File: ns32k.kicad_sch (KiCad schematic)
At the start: 49 parts, among them SW2 SW_DIP_x04, U1 NS32201, U10 74AHC373, U11 74AHC373, U12 74AHC138, U13 AS6C6416-55, U15 MX29LV040C, U16 MX29LV040C, U19 74AHC32, U20 74AHC1GU04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

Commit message: layout ICU buffering
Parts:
- added C58: 0.1µF, Capacitor_SMD:C_0402_1005Metric, symbol Device:C_Small
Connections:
- net +3V3: now also C58.1
- net D0: no longer U22.18 (B0), U5.19 (D0)
- net D1: no longer U22.17 (B1), U5.18 (D1)
- net D2: no longer U22.16 (B2), U5.17 (D2)
- net D3: no longer U22.15 (B3), U5.16 (D3)
- net D4: no longer U22.14 (B4), U5.15 (D4)
- net D5: no longer U22.13 (B5), U5.14 (D5)
- net D6: no longer U22.12 (B6), U5.13 (D6)
- net D7: no longer U22.11 (B7), U5.12 (D7)
- net GND: now also C58.2
- new net: U22.11 (B7), U5.12 (D7)
- new net: U22.12 (B6), U5.13 (D6)
- new net: U22.13 (B5), U5.14 (D5)
- new net: U22.14 (B4), U5.15 (D4)
- new net: U22.15 (B3), U5.16 (D3)
- new net: U22.16 (B2), U5.17 (D2)
- new net: U22.17 (B1), U5.18 (D1)
- new net: U22.18 (B0), U5.19 (D0)
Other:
- moved on the sheet: U19B, U20

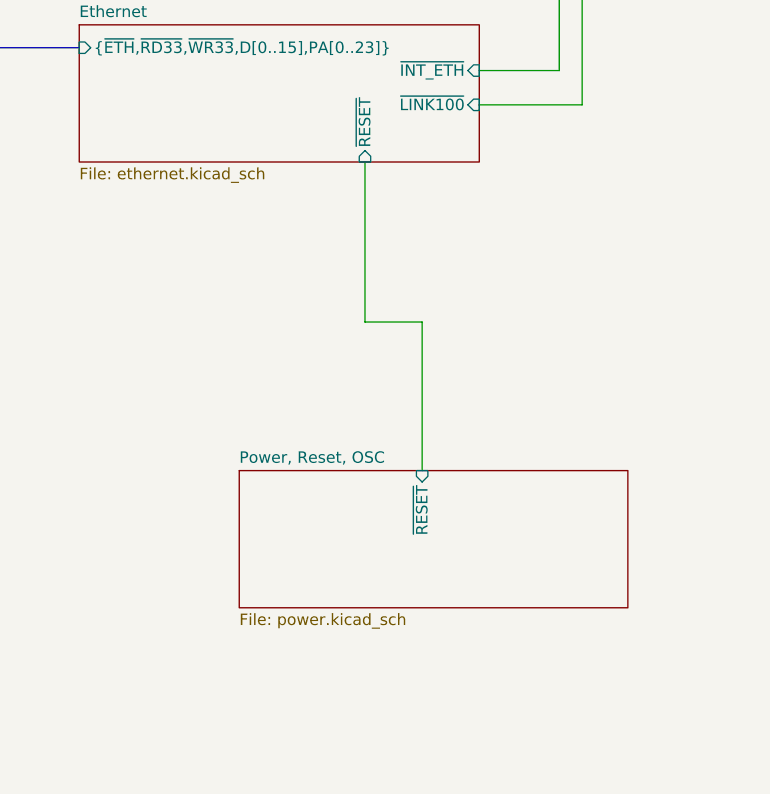
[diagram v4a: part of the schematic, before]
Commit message: add 33uF 1206 16V reservoir cap to 5V
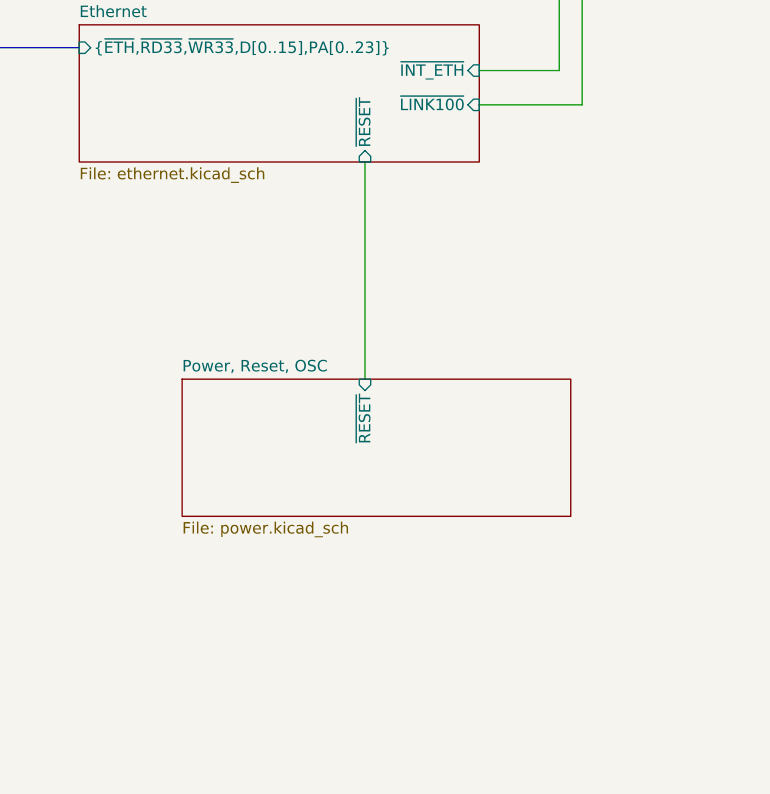
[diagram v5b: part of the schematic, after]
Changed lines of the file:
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@@
 	(wire
 		(pts
-			(xy 359.41 212.09) (xy 359.41 194.31)
+			(xy 359.41 194.31) (xy 359.41 218.44)
 		)
 		(stroke
@@
 	(wire
 		(pts
-			(xy 365.76 212.09) (xy 359.41 212.09)
-		)
-		(stroke
-			(width 0)
-			(type default)
-		)
-	)
-	(wire
-		(pts
 			(xy 187.96 91.44) (xy 187.96 93.98)
 		)
@@
 		)
 	)
-	(wire
-		(pts
-			(xy 365.76 228.6) (xy 365.76 212.09)
-		)
-		(stroke
-			(width 0)
-			(type default)
-		)
-	)
 	(bus
 		(pts
@@
 	(label "PA5"
 		(at 300.99 77.47 180)
+		(fields_autoplaced yes)
 		(effects
 			(font
@@
 	(label "~{ICU}"
 		(at 298.45 57.15 180)
+		(fields_autoplaced yes)
 		(effects
 			(font
@@
 	(label "~{ICU}"
 		(at 287.02 74.93 0)
+		(fields_autoplaced yes)
 		(effects
 			(font
@@
 	(label "~{ICU}"
 		(at 232.41 158.75 0)
+		(fields_autoplaced yes)
 		(effects
 			(font
@@
 	(label "~{DBE}"
 		(at 238.76 73.66 90)
+		(fields_autoplaced yes)
 		(effects
 			(font
@@
 	)
 	(sheet
-		(at 345.44 228.6)
+		(at 339.09 218.44)
 		(size 43.18 15.24)
 		(fields_autoplaced yes)
@@
 		)
 		(property "Sheetname" "Power, Reset, OSC"
-			(at 345.44 227.8884 0)
+			(at 339.09 217.7284 0)
 			(effects
 				(font
@@
 		)
 		(property "Sheetfile" "power.kicad_sch"
-			(at 345.44 244.4246 0)
+			(at 339.09 234.2646 0)
 			(effects
 				(font
@@
 		)
 		(pin "~{RESET}" input
-			(at 365.76 228.6 90)
+			(at 359.41 218.44 90)
 			(effects
 				(font

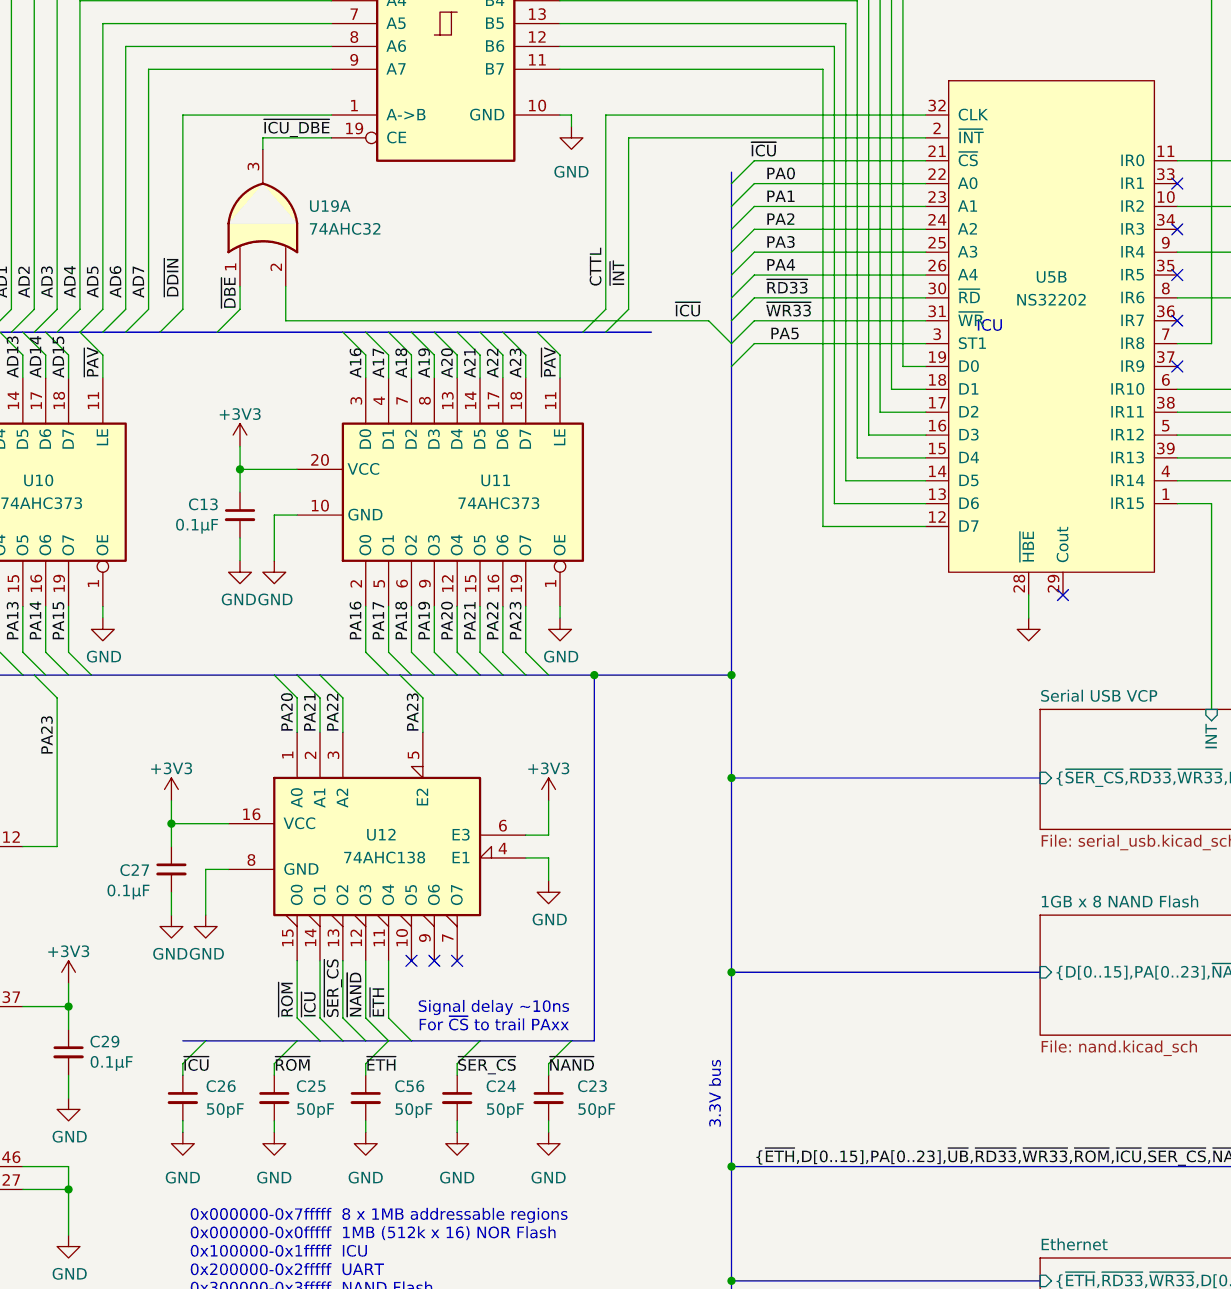
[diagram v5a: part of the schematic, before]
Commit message: fix ICU addressing error
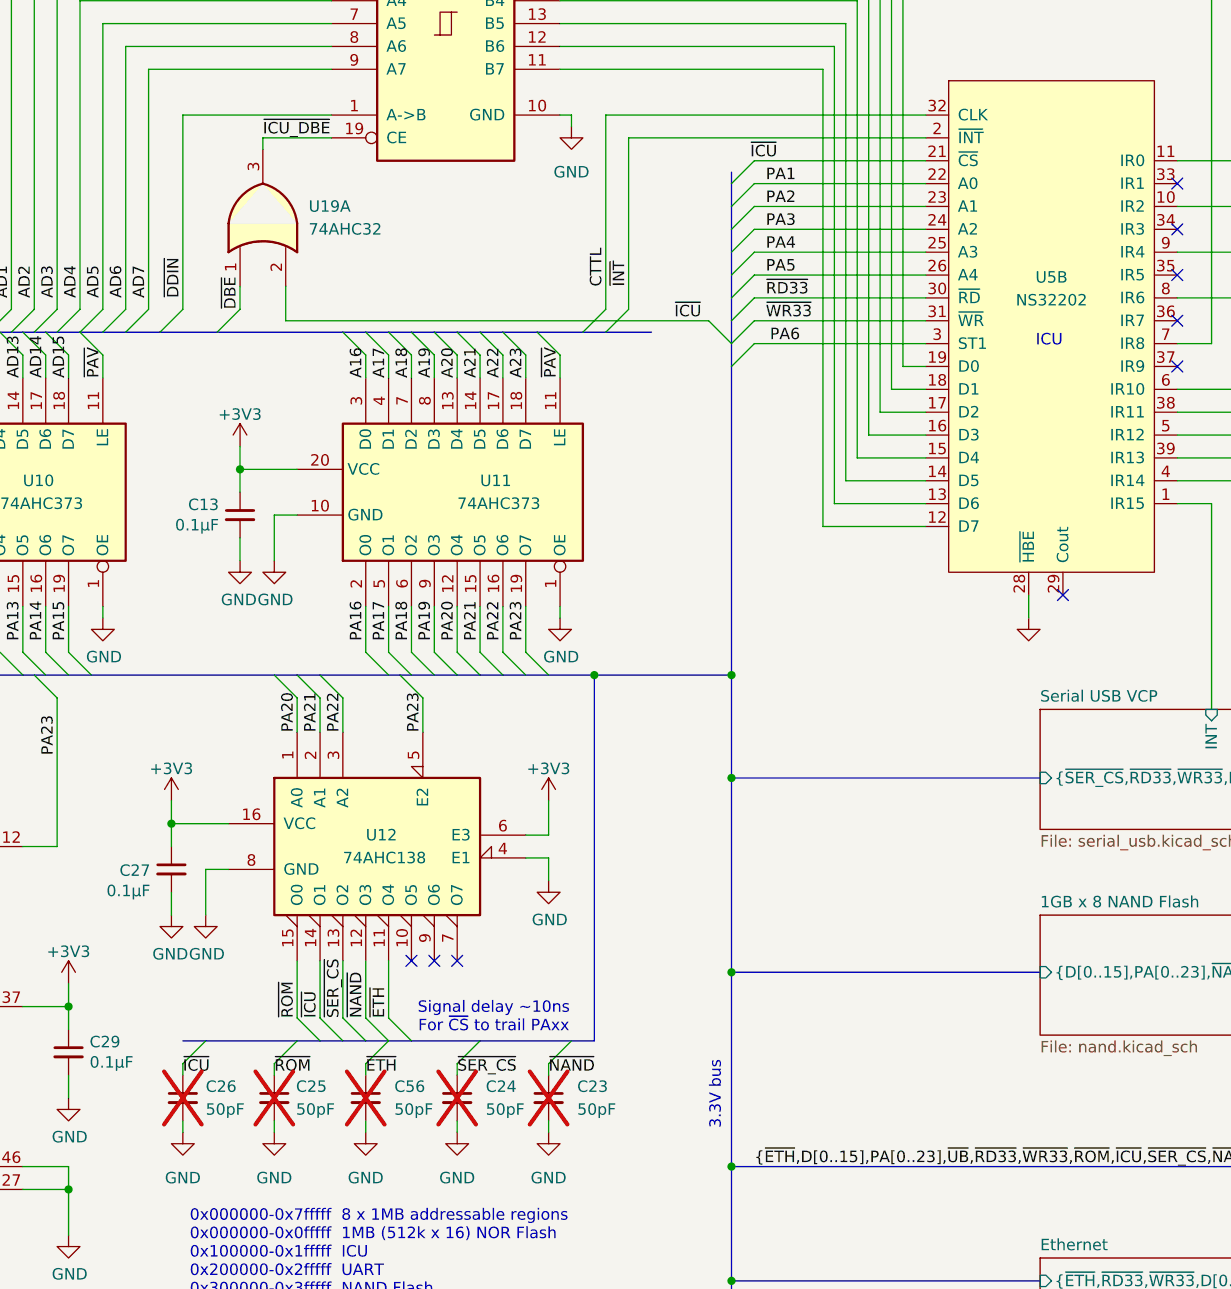
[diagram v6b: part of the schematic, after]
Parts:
- C23, C24, C25, C26, C56: now not fitted
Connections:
- net PA0: no longer U5.22 (A0)
- net PA1: now also U5.22 (A0); no longer U5.23 (A1)
- net PA2: now also U5.23 (A1); no longer U5.24 (A2)
- net PA3: now also U5.24 (A2); no longer U5.25 (A3)
- net PA4: now also U5.25 (A3); no longer U5.26 (A4)
- net PA5: now also U5.26 (A4); no longer U5.3 (ST1)
- net PA6: now also U5.3 (ST1)
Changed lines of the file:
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@@
 	(text "ICU"
 		(exclude_from_sim no)
-		(at 322.072 75.692 0)
+		(at 328.676 77.216 0)
 		(effects
 			(font
@@
 		)
 	)
-	(label "PA4"
+	(label "PA5"
 		(at 297.18 69.85 0)
 		(fields_autoplaced yes)
@@
 		)
 	)
-	(label "PA5"
+	(label "PA6"
 		(at 300.99 77.47 180)
 		(fields_autoplaced yes)
@@
 		)
 	)
-	(label "PA2"
+	(label "PA3"
 		(at 297.18 64.77 0)
 		(fields_autoplaced yes)
@@
 		)
 	)
-	(label "PA3"
+	(label "PA4"
 		(at 297.18 67.31 0)
 		(fields_autoplaced yes)
@@
 		)
 	)
-	(label "PA0"
+	(label "PA1"
 		(at 297.18 59.69 0)
 		(fields_autoplaced yes)
@@
 		)
 	)
-	(label "PA1"
+	(label "PA2"
 		(at 297.18 62.23 0)
 		(fields_autoplaced yes)
@@
 		(in_bom yes)
 		(on_board yes)
-		(dnp no)
+		(dnp yes)
 		(property "Reference" "C56"
 			(at 255.905 160.0262 0)
@@
 		(in_bom yes)
 		(on_board yes)
-		(dnp no)
+		(dnp yes)
 		(property "Reference" "C24"
 			(at 266.065 160.0262 0)
@@
 		(in_bom yes)
 		(on_board yes)
-		(dnp no)
+		(dnp yes)
 		(property "Reference" "C26"
 			(at 234.95 160.02 0)
@@
 		(in_bom yes)
 		(on_board yes)
-		(dnp no)
+		(dnp yes)
 		(property "Reference" "C25"
 			(at 244.983 160.02 0)
@@
 		(in_bom yes)
 		(on_board yes)
-		(dnp no)
+		(dnp yes)
 		(fields_autoplaced yes)
 		(property "Reference" "C23"
